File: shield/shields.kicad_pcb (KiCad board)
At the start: 2 copper layers, 40.4 x 95.7 mm, 8 parts

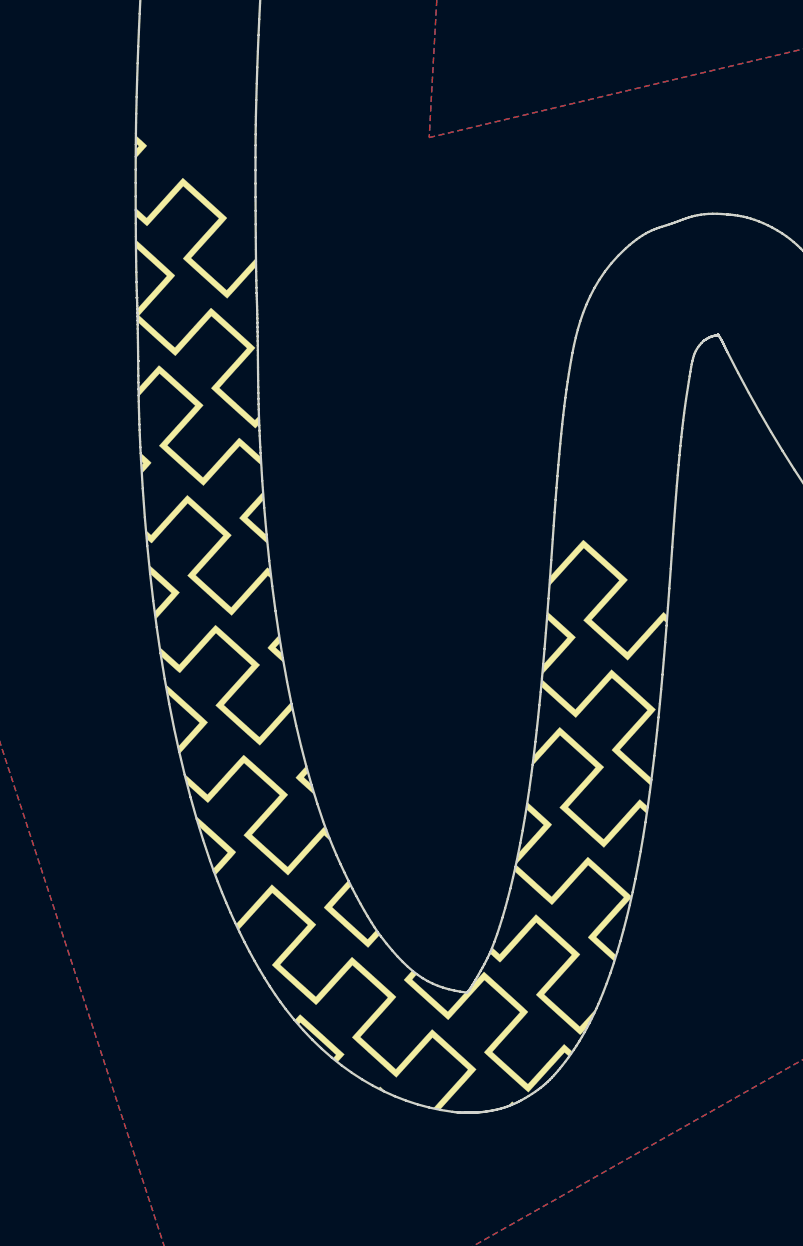
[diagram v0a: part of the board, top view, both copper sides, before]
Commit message: Add part for shield art
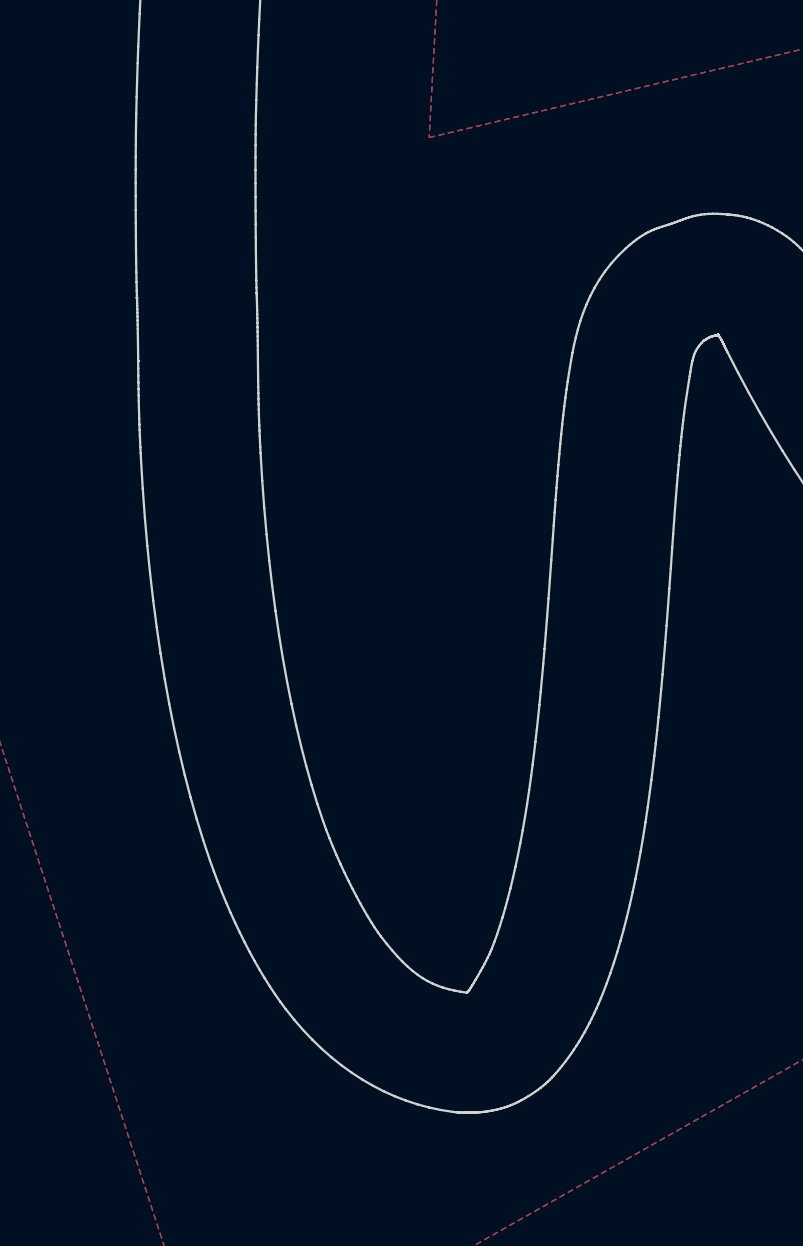
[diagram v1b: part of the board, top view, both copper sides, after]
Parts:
- removed the G*** at (0.00, 0.00) (x6)
- G***: value LOGO -> shield-sqwv-silk; footprint LOGO -> Swadge_Parts:shield-sqwv-metal
